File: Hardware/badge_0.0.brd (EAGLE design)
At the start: 100 x 50 mm, 43 parts, among them CON1 PH_2, IC1 CP2102, SW1 MK12C02, SW2 MK12C02, U4 MCP73832T-2DCI/OT

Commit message: before teardown
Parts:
- added J3: (no value), SparkFun-Connectors:1X12
- added J4: (no value), SparkFun-Connectors:1X08_ROUND
- added J5: (no value), SparkFun-Connectors:1X05
- added U1: (no value), esp8266modules:ESP12-SMD
- moved J8 70.4 mm to (91.6, 72.3)
- moved U$5 27.5 mm to (65.5, 35.8)
- moved J10 10.3 mm to (99.5, 58.1)
- moved U6 9.91 mm to (85.6, 34.3), turned to 270 degrees
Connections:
- net ADC: now also J3.2
- net CH_PD: now also J3.3
- net CS0: now also J3.12
- net GPIO0: now also J4.3
- net GPIO10: now also J4.8
- net GPIO12/SPI_SO: now also J3.4
- net GPIO13/SPI_SI: now also J3.5
- net GPIO14/SPI_CLK/SCL: now also J3.6
- net GPIO15/SPI_CS: now also J3.7
- net GPIO16: now also J3.8
- net GPIO2/SDA: now also J4.4
- net GPIO4: now also J4.5
- net GPIO5: now also J4.6
- net GPIO9: now also J4.7
- net MISO: now also J3.11
- net MOSI: now also J3.10
- net RESET: now also J3.1
- net RX: now also J4.2
- net SCLK: now also J3.9
- net TX: now also J4.1
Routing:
- net GND: track 424.7 -> 266.2 mm, vias 100 -> 97
- net GPIO15/SPI_CS: track 131.3 -> 9.68 mm, vias 9 -> 2
- net GPIO2/SDA: track 92.1 -> 0.00 mm, vias 3 -> 0
- net VCC: track 220.4 -> 137.1 mm, vias 6 -> 5
- net GPIO14/SPI_CLK/SCL: track 116.5 -> 34.0 mm, vias 2 -> 0
- net GPIO13/SPI_SI: track 110.1 -> 34.4 mm, vias 1 -> 0
- net GPIO12/SPI_SO: track 108.7 -> 34.8 mm, vias 1 -> 0
- net GPIO16: track 66.5 -> 1.38 mm, vias 1 -> 0
- net CH_PD: track 59.3 -> 0.11 mm, vias 2 -> 0
- net GPIO4: track 59.1 -> 0.00 mm, vias 3 -> 0
- net GPIO5: track 55.7 -> 0.00 mm, vias 3 -> 0
- net GPIO0: track 56.8 -> 3.01 mm, vias 2 -> 0
- net RESET: track 84.6 -> 38.5 mm, vias 5 -> 2
- net ADC: track 41.5 -> 0.00 mm, vias 1 -> 0
- net RX: track 35.9 -> 5.70 mm
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
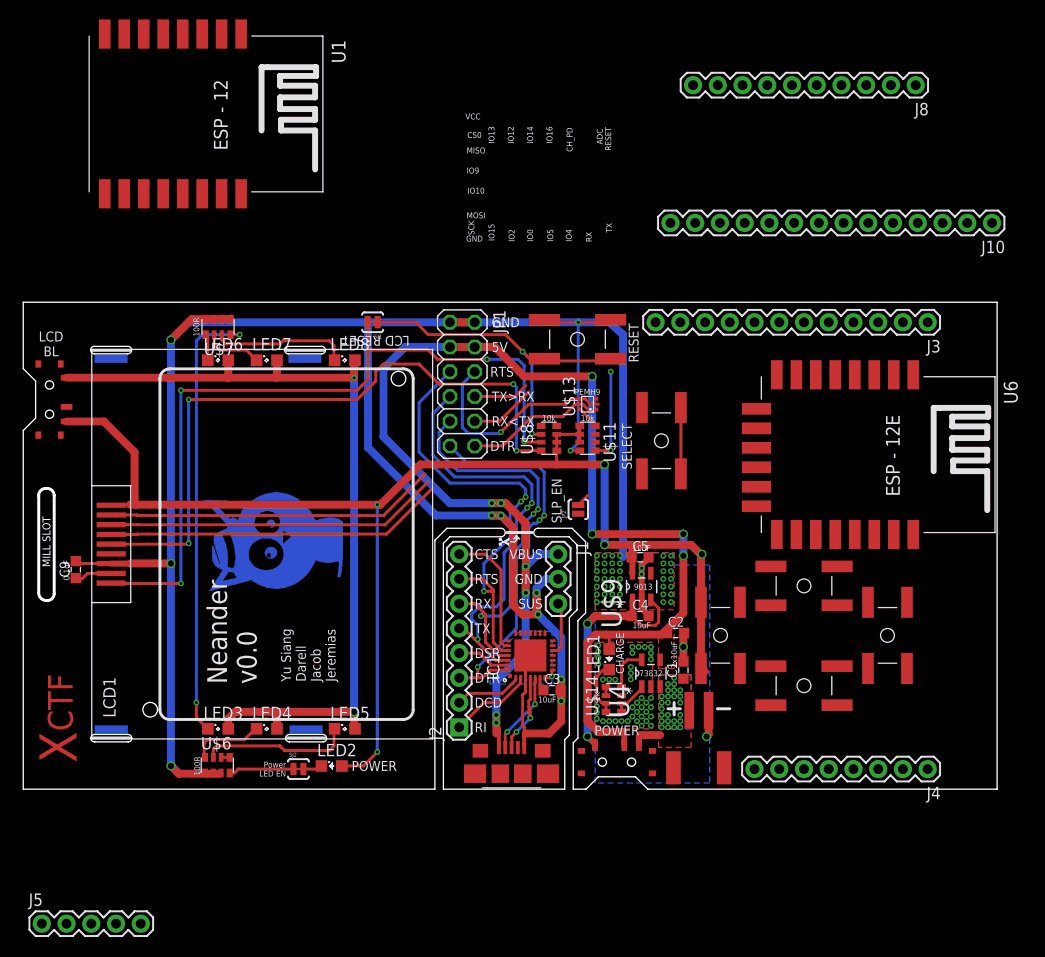
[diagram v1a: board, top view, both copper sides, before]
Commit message: moved ESP to the opposite end w.r.t. LCD
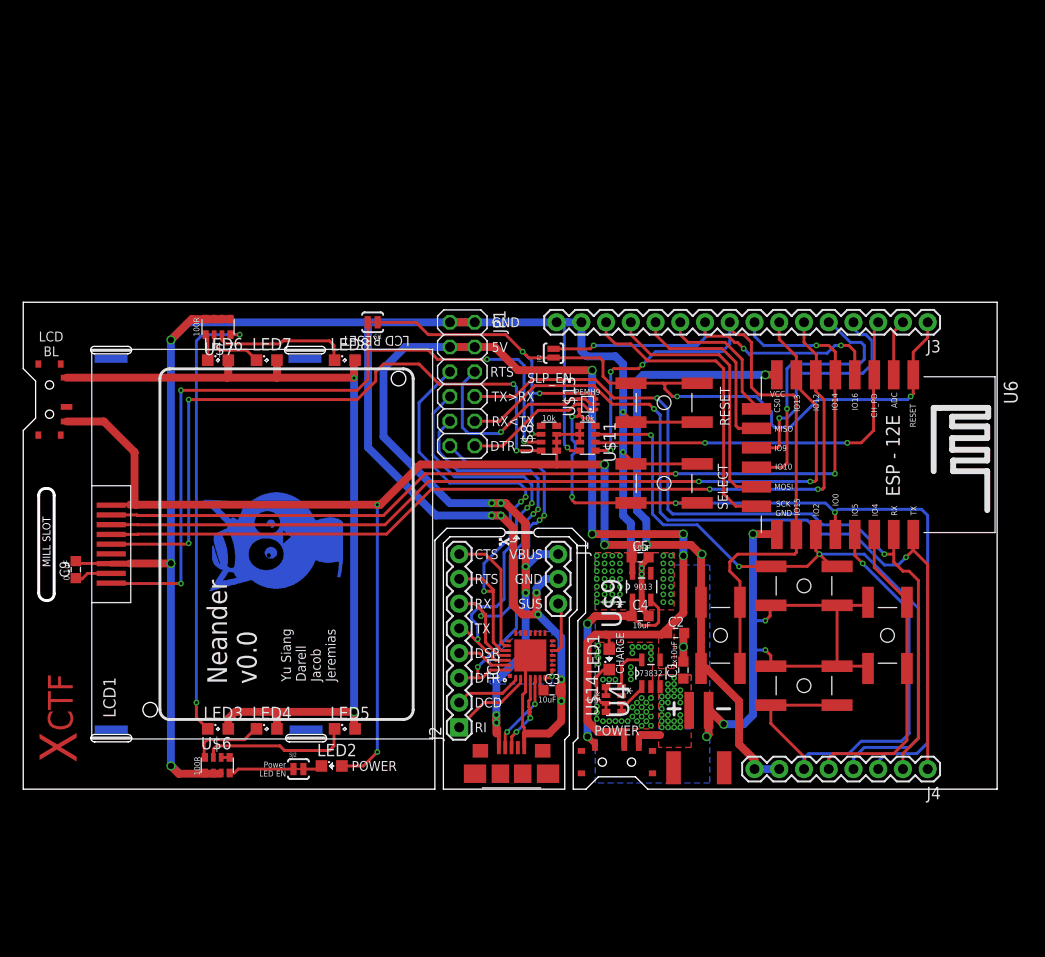
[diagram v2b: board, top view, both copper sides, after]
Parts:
- removed J10: (no value), SparkFun-Connectors:1X14
- removed J5: (no value), SparkFun-Connectors:1X05
- removed J8: (no value), SparkFun-Connectors:1X10
- removed U1: (no value), esp8266modules:ESP12-SMD
- J3: device SparkFun-Connectors:1X12 -> SparkFun-Connectors:1X16
- moved JP2 16.2 mm to (54.5, 44.8)
- moved U$12 11.0 mm to (65.8, 39.7), turned to 90 degrees
- moved U$5 4.39 mm to (65.8, 31.4), turned to 270 degrees
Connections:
- net ADC: no longer J8.7
- net CH_PD: no longer J8.6
- net CS0: now also J3.11; no longer J10.1, J3.12
- net GND: now also J3.15, J3.16; no longer J10.11, J10.12, J8.8
- net GPIO0: no longer J10.10
- net GPIO10: now also J3.5; no longer J10.5, J4.8
- net GPIO12/SPI_SO: now also J3.6; no longer J3.4, J8.5
- net GPIO13/SPI_SI: now also J3.7; no longer J3.5, J8.4
- net GPIO14/SPI_CLK/SCL: now also J3.8; no longer J3.6, J8.3
- net GPIO15/SPI_CS: now also J3.9; no longer J3.7, J8.2
- net GPIO16: now also J3.10; no longer J3.8, J8.1
- net GPIO2/SDA: now also U$2.P$2, U$2.P$3; no longer J10.9, U$3.P$2, U$3.P$3
- net GPIO4: now also U$4.P$2, U$4.P$3; no longer J10.8, U$2.P$2, U$2.P$3
- net GPIO5: now also U$3.P$2, U$3.P$3; no longer J10.7, U$4.P$2, U$4.P$3
- net GPIO9: now also J3.4; no longer J10.6, J4.7
- net MISO: now also J3.12; no longer J10.2, J3.11
- net MOSI: now also J3.13; no longer J10.3, J3.10
- net RX: no longer J10.13
- net SCLK: now also J3.14; no longer J10.4, J3.9
- net TX: no longer J10.14
- net VCC: now also J4.7, J4.8; no longer J8.10, J8.9
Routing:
- net GPIO0: track 3.01 -> 84.9 mm, vias 0 -> 4
- net TX: track 6.81 -> 85.6 mm, vias 0 -> 2
- net RX: track 5.70 -> 83.4 mm, vias 0 -> 2
- net GPIO2/SDA: track 0.00 -> 72.7 mm, vias 0 -> 3
- net GPIO14/SPI_CLK/SCL: track 34.0 -> 99.0 mm, vias 0 -> 3
- net GPIO15/SPI_CS: track 9.68 -> 72.9 mm, vias 2 -> 3
- net GND: track 266.2 -> 328.5 mm, vias 97 -> 102
- net GPIO12/SPI_SO: track 34.8 -> 93.1 mm, vias 0 -> 2
- net GPIO13/SPI_SI: track 34.4 -> 92.1 mm, vias 0 -> 2
- net RESET: track 38.5 -> 90.9 mm, vias 2 -> 5
- net GPIO5: track 0.00 -> 50.5 mm, vias 0 -> 1
- net VCC: track 137.1 -> 184.0 mm, vias 5 -> 7
- net CH_PD: track 0.11 -> 40.4 mm, vias 0 -> 2
- net GPIO16: track 1.38 -> 38.2 mm, vias 0 -> 3
- net GPIO4: track 0.00 -> 32.4 mm
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
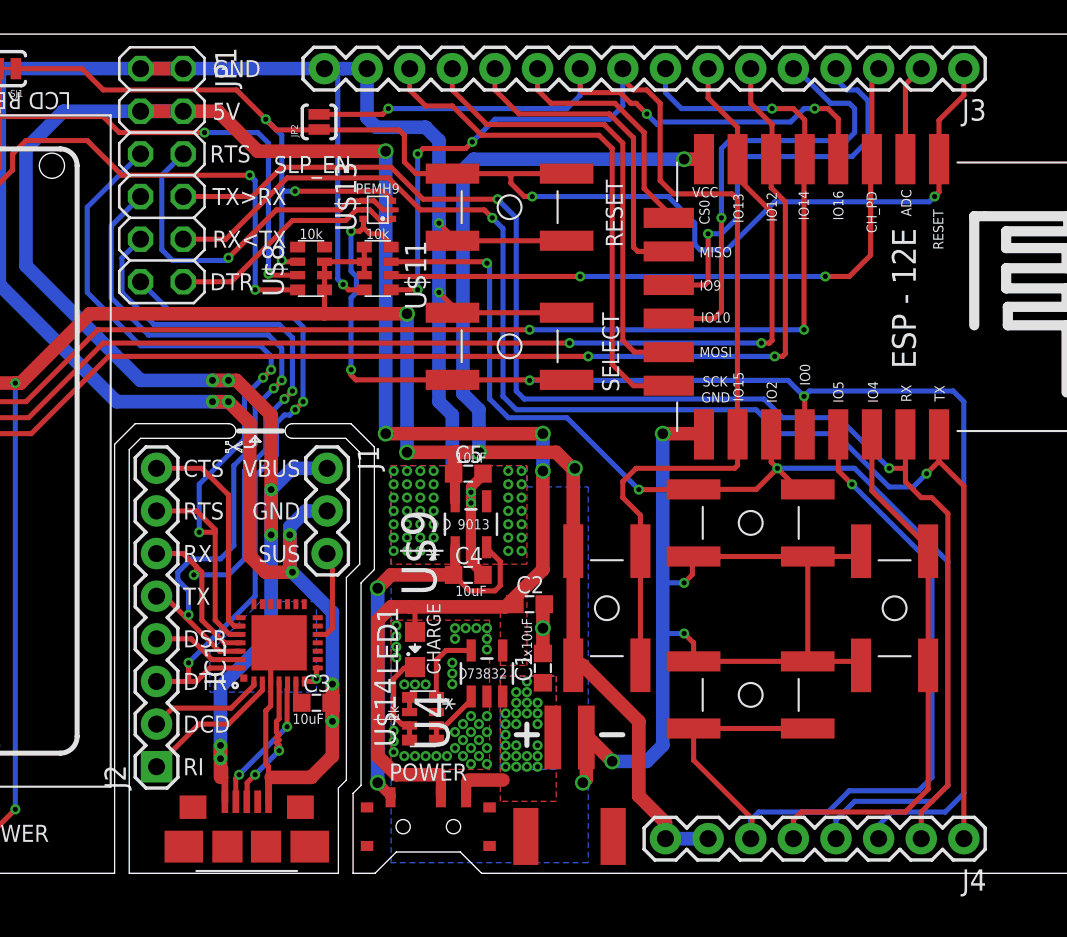
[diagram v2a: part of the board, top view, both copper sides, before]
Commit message: Added !susp to serial headers. Rerouted many traces
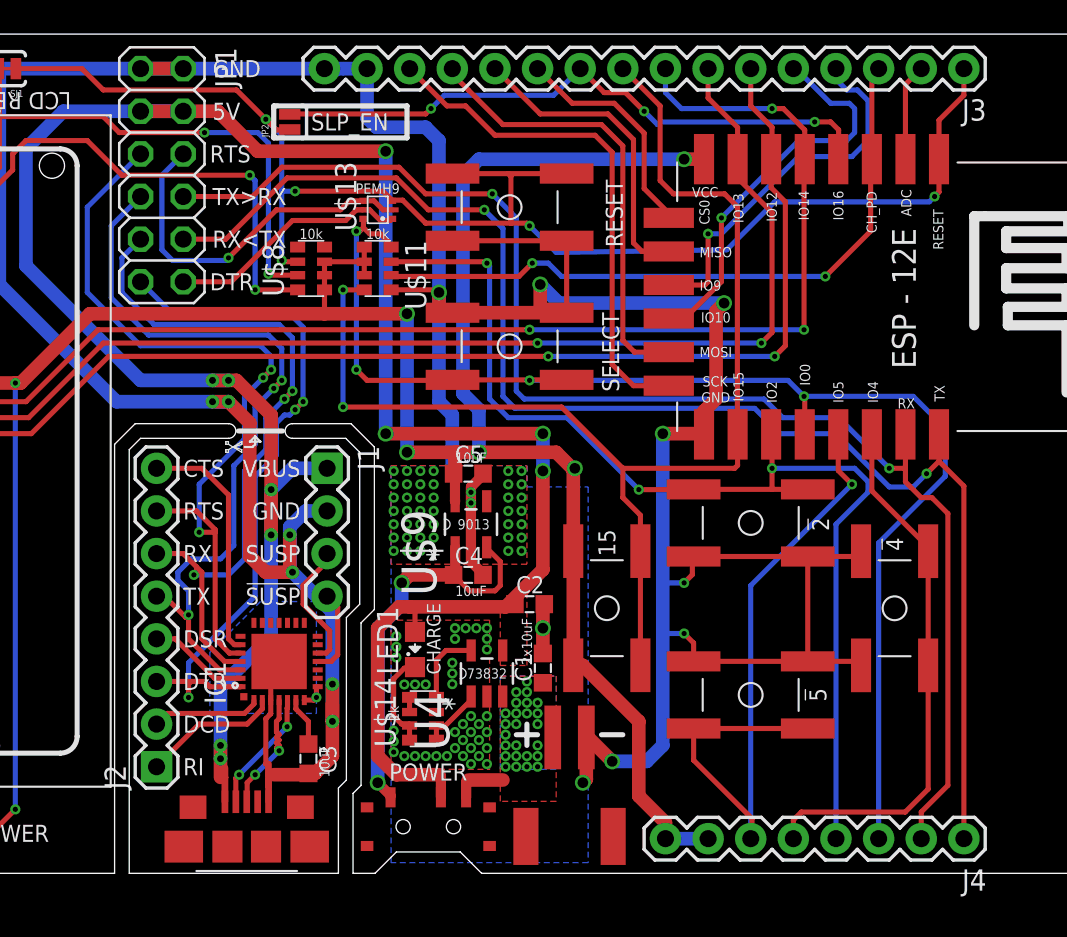
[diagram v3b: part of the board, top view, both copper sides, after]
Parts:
- J1: device SparkFun-Connectors:1X03 -> SparkFun-Connectors:1X04
- moved C3 3.37 mm to (53.8, 6.83), turned to 270 degrees
- moved JP2 1.75 mm to (52.7, 44.8)
- moved IC1 1.11 mm to (52.1, 12.6)
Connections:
- new net S_!SUSP: IC1.11, J1.4
- net GND: now also U$11.5; no longer U$11.4
- net GPIO15/SPI_CS: now also U$11.4; no longer U$11.5
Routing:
- net GND: track 328.5 -> 341.9 mm, vias 102 -> 101
- net GPIO5: track 50.5 -> 41.8 mm
- net GPIO2/SDA: track 72.7 -> 67.1 mm
- net GPIO0: track 84.9 -> 79.2 mm
- net S_!SUSP: track 0.00 -> 5.11 mm
- net GPIO10: track 27.4 -> 24.0 mm
- net RESET: track 90.9 -> 87.6 mm
- net S_SUSP: track 5.61 -> 7.77 mm
- net GPIO9: track 24.6 -> 22.6 mm
- net S_DTR: track 40.3 -> 42.0 mm
- net N$20: track 1.42 -> 2.93 mm
- net S_TXD: track 44.6 -> 45.8 mm
- net S_RXD: track 42.1 -> 43.2 mm
- net D-: track 8.45 -> 7.33 mm
- net S_CTS: track 13.3 -> 14.4 mm
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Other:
- outline, holes or cut-outs redrawn
- board text added: "!2"
- board text added: "!4"
- board text added: "!5"
- board text added: "!SUSP"
- board text added: "15"
- board text added: "SUSP"
- board text removed: "SUS"

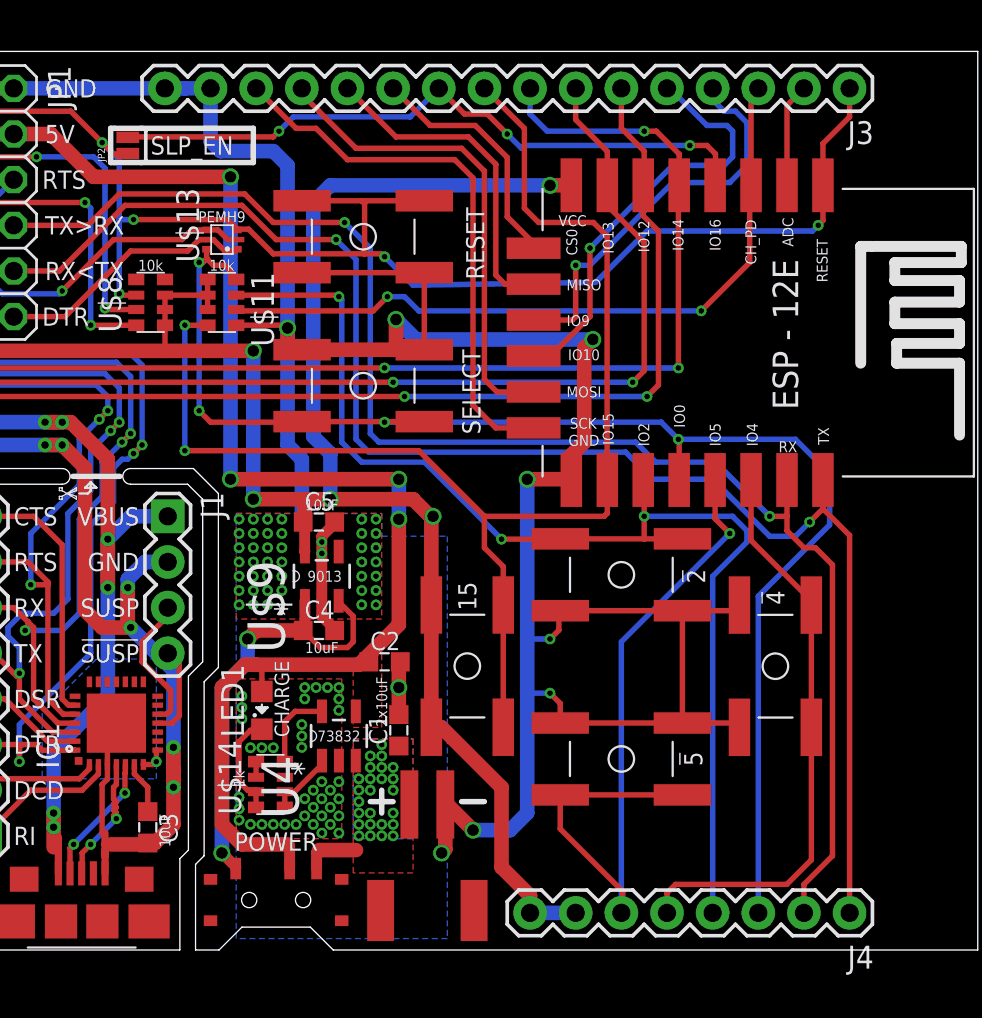
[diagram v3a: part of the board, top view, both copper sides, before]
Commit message: Rerouted stuff. Added new power supply headers near LCD
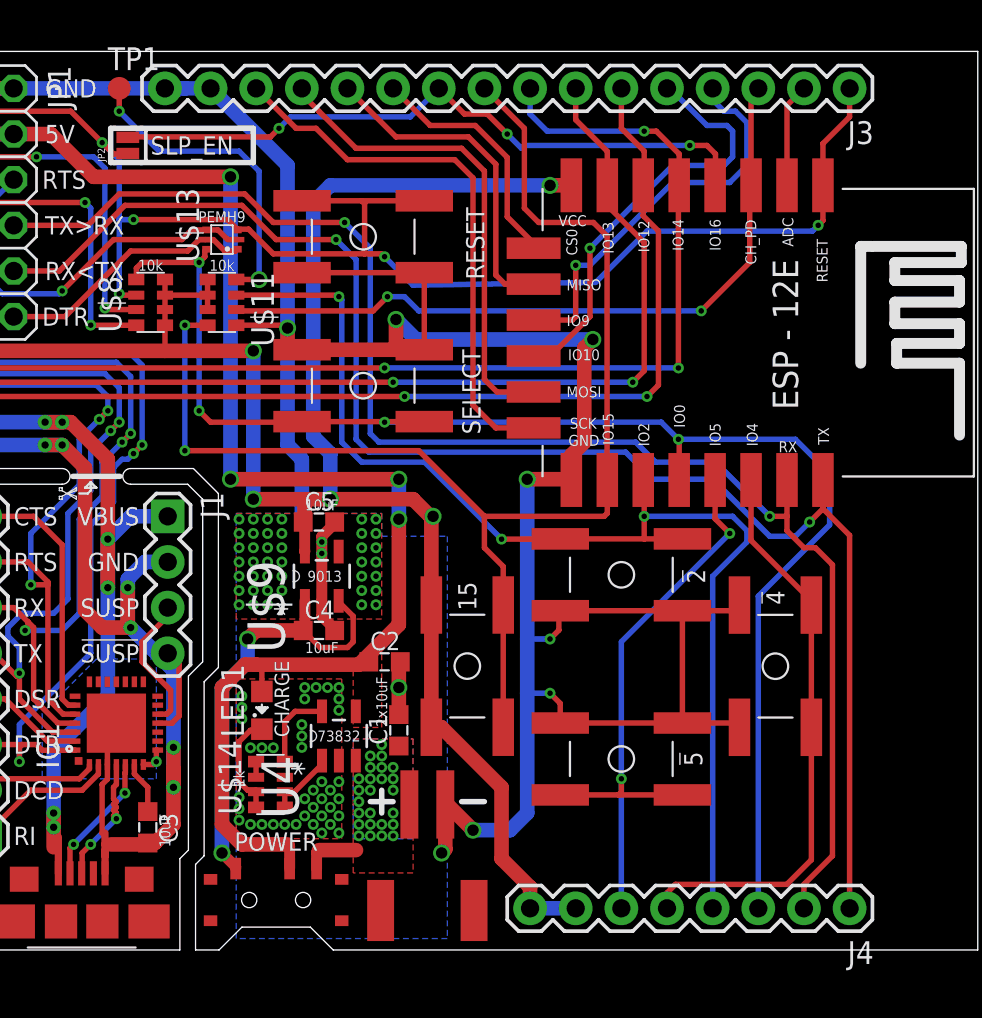
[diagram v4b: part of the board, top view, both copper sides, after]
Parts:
- added TP1: PTR1B1,27, testpad:B1,27
- moved J4 0.25 mm to (92.9, 2.32)
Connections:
- new net N$3: TP1.TP, U$11.8
- net GPIO0: now also U$8.5; no longer U$11.8
- net VCC: now also U$8.4
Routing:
- net N$3: track 0.00 -> 17.7 mm, vias 0 -> 2
- net GPIO5: track 41.8 -> 34.4 mm, vias 1 -> 2
- net GND: track 341.9 -> 340.1 mm
- net GPIO0: track 79.2 -> 80.3 mm
- net VCC: track 183.8 -> 184.4 mm

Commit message: May not have saved for last commit
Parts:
- added J5, J6: (no value), SparkFun-Connectors:1X04
- moved U$7 2.70 mm to (22.7, 47.5)
- moved U$6 1.59 mm to (21.5, 2.46)
- moved J4 0.10 mm to (92.9, 2.22)
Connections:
- net GND: now also J5.3, J5.4, J6.3, J6.4
- net VCC: now also J5.1, J5.2, J6.1, J6.2
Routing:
- net VCC: track 184.4 -> 247.4 mm, vias 7 -> 8
- net GND: track 340.1 -> 351.6 mm
- net N$14: track 46.0 -> 48.7 mm
- net N$7: track 6.03 -> 3.33 mm
- net N$8: track 14.1 -> 11.4 mm
- net N$22: track 3.02 -> 4.85 mm
- net N$12: track 7.67 -> 6.08 mm
- net N$15: track 6.72 -> 5.13 mm
- net N$13: track 15.5 -> 14.0 mm
